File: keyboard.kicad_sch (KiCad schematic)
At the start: 77 parts

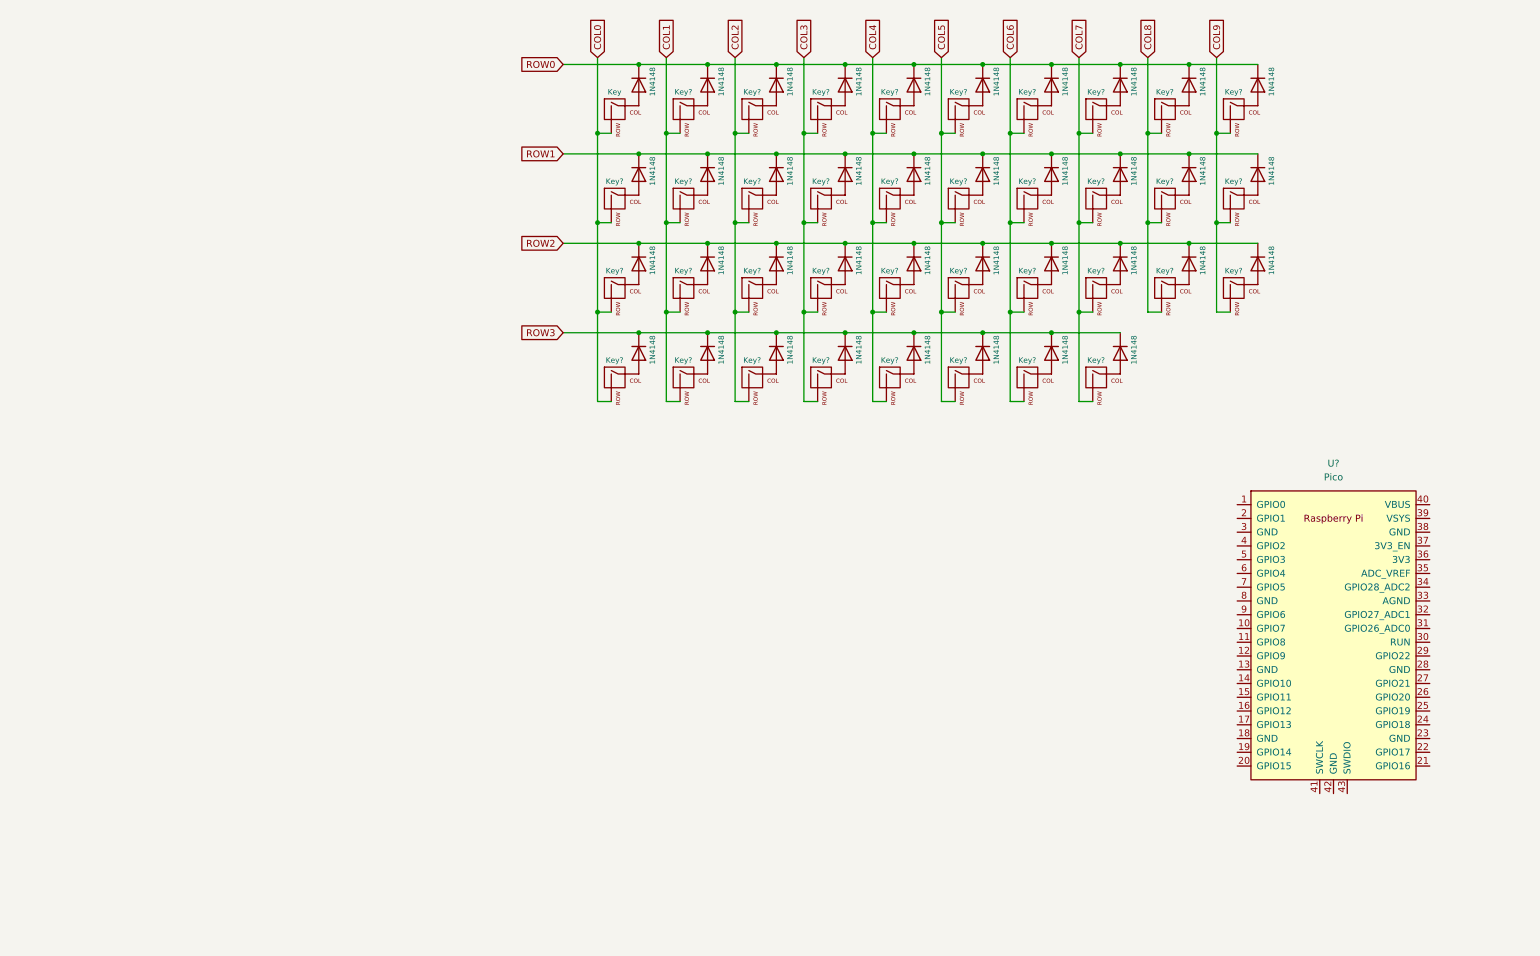
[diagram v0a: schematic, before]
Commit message: updated schematic to dual pallel switches
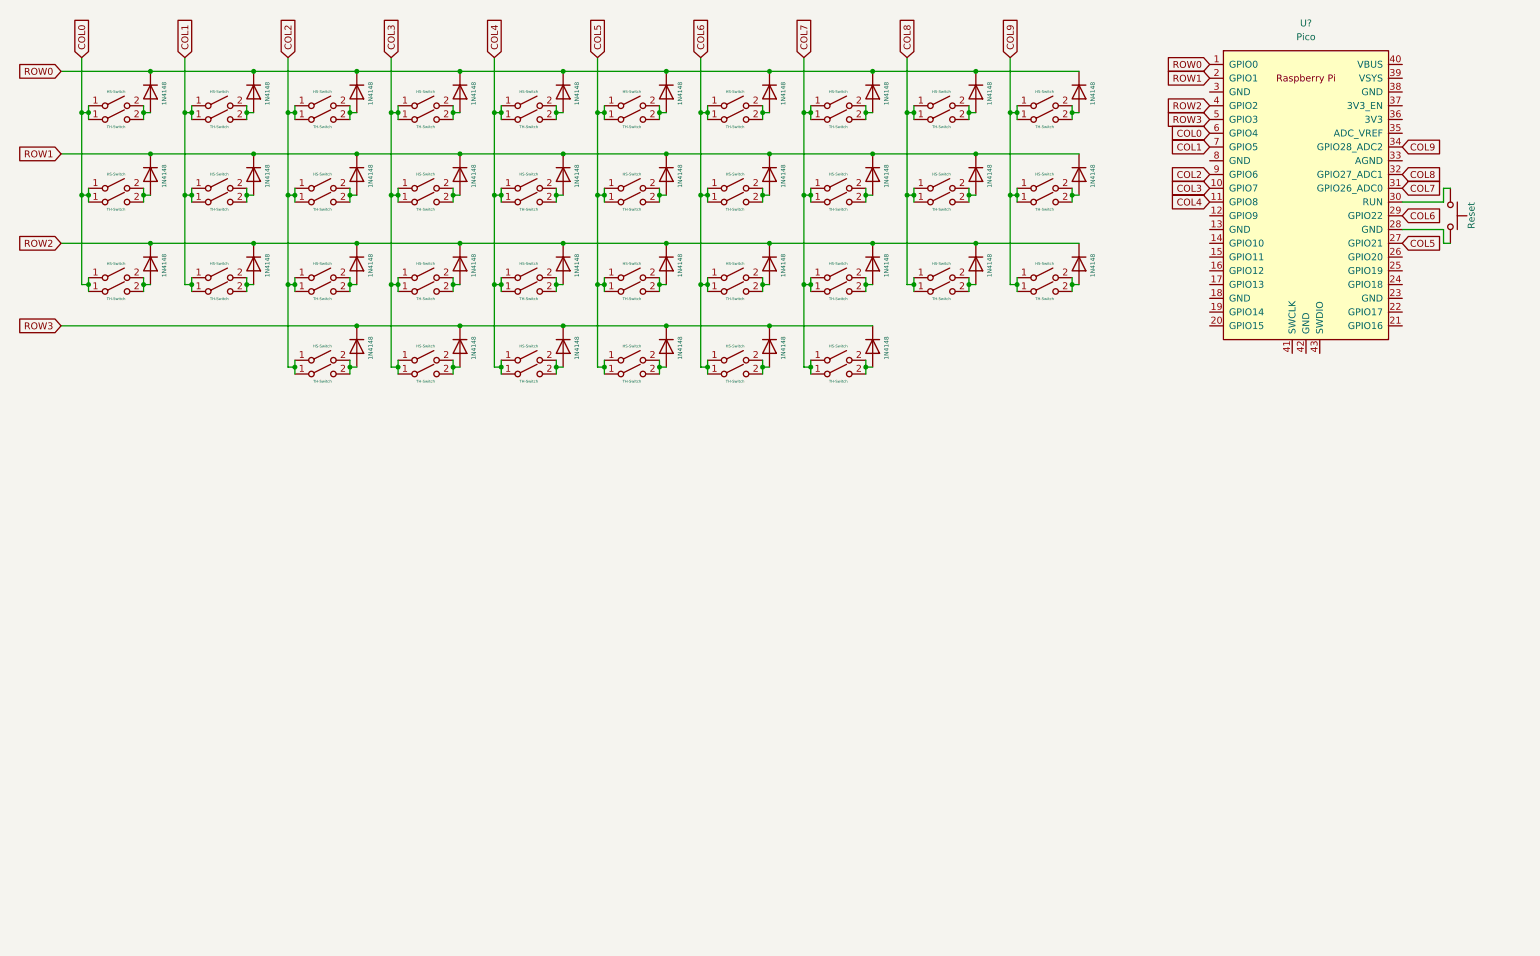
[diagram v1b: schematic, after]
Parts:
- removed D? (x38): 1N4148, Diode_THT:D_DO-35_SOD27_P7.62mm_Horizontal, symbol Diode:1N4148
- removed Key, Key? (x37): no-led, symbol MX_Alps_Hybrid:MX-NoLED
- added D? (x36): 1N4148, Diode_THT:D_DO-35_SOD27_P7.62mm_Horizontal, symbol Diode:1N4148
- added Reset: SW_Push, symbol Switch:SW_Push
- added SW? (x36): HS-Switch, symbol Switch:SW_SPST
- added SW? (x36): TH-Switch, symbol Switch:SW_SPST
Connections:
- net COL0: now also U?.6 (GPIO4), SW?.1 (A), SW?.1 (A), SW?.1 (A), SW?.1 (A), SW?.1 (A), SW?.1 (A)
- net COL1: now also U?.7 (GPIO5), SW?.1 (A), SW?.1 (A), SW?.1 (A), SW?.1 (A), SW?.1 (A), SW?.1 (A)
- net COL2: now also U?.9 (GPIO6), SW?.1 (A), SW?.1 (A), SW?.1 (A), SW?.1 (A), SW?.1 (A), SW?.1 (A), SW?.1 (A), SW?.1 (A)
- net COL3: now also U?.10 (GPIO7), SW?.1 (A), SW?.1 (A), SW?.1 (A), SW?.1 (A), SW?.1 (A), SW?.1 (A), SW?.1 (A), SW?.1 (A)
- net COL4: now also U?.11 (GPIO8), SW?.1 (A), SW?.1 (A), SW?.1 (A), SW?.1 (A), SW?.1 (A), SW?.1 (A), SW?.1 (A), SW?.1 (A)
- net COL5: now also U?.27 (GPIO21), SW?.1 (A), SW?.1 (A), SW?.1 (A), SW?.1 (A), SW?.1 (A), SW?.1 (A), SW?.1 (A), SW?.1 (A)
- net COL6: now also U?.29 (GPIO22), SW?.1 (A), SW?.1 (A), SW?.1 (A), SW?.1 (A), SW?.1 (A), SW?.1 (A), SW?.1 (A), SW?.1 (A)
- net COL7: now also U?.31 (GPIO26_ADC0), SW?.1 (A), SW?.1 (A), SW?.1 (A), SW?.1 (A), SW?.1 (A), SW?.1 (A), SW?.1 (A), SW?.1 (A)
- net COL8: now also U?.32 (GPIO27_ADC1), SW?.1 (A), SW?.1 (A), SW?.1 (A), SW?.1 (A), SW?.1 (A), SW?.1 (A)
- net COL9: now also U?.34 (GPIO28_ADC2), SW?.1 (A), SW?.1 (A), SW?.1 (A), SW?.1 (A), SW?.1 (A), SW?.1 (A)
- net ROW0: now also U?.1 (GPIO0), D?.1 (K), D?.1 (K), D?.1 (K), D?.1 (K), D?.1 (K), D?.1 (K), D?.1 (K), D?.1 (K), D?.1 (K), D?.1 (K)
- net ROW1: now also U?.2 (GPIO1), D?.1 (K), D?.1 (K), D?.1 (K), D?.1 (K), D?.1 (K), D?.1 (K), D?.1 (K), D?.1 (K), D?.1 (K), D?.1 (K)
- net ROW2: now also U?.4 (GPIO2), D?.1 (K), D?.1 (K), D?.1 (K), D?.1 (K), D?.1 (K), D?.1 (K), D?.1 (K), D?.1 (K), D?.1 (K), D?.1 (K)
- net ROW3: now also U?.5 (GPIO3), D?.1 (K), D?.1 (K), D?.1 (K), D?.1 (K), D?.1 (K), D?.1 (K)
- net at U?.28 (GND): now also Reset.2
- net at U?.30 (RUN): now also Reset.1
- new net: D?.2 (A), SW?.2 (B), SW?.2 (B) (x36)
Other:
- moved on the sheet: U?

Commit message: wired up 2 oled screens and 2 rotary encoders and cleaned up the schematic
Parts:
- added 10K (x6): R, symbol Device:R
- added Brd?: OLEDR, symbol SSD1306-128x64_OLED:SSD1306
- added Brd?: OLEDL, symbol SSD1306-128x64_OLED:SSD1306
- added SW?: RER, symbol Device:RotaryEncoder_Switch
- added SW?: REL, symbol Device:RotaryEncoder_Switch
- U?: value Pico -> Pi Pico
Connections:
- net REL-S1: now reaches U?.12 (GPIO9)
- net REL-S1: now also 10K.1, SW?.S1
- net REL-A: now reaches U?.14 (GPIO10)
- net REL-A: now also 10K.2, SW?.A
- net REL-B: now reaches U?.15 (GPIO11)
- net REL-B: now also 10K.2, SW?.B
- net SDAOLEDL: now reaches U?.16 (GPIO12)
- net SDAOLEDL: now also Brd?.4 (SDA)
- net SCLOLEDL: now reaches U?.17 (GPIO13)
- net SCLOLEDL: now also Brd?.3 (SCL)
- net SDAOLEDR: now reaches U?.21 (GPIO16)
- net SDAOLEDR: now also Brd?.4 (SDA)
- net SCLOLEDR: now reaches U?.22 (GPIO17)
- net SCLOLEDR: now also Brd?.3 (SCL)
- net REGND: now reaches U?.23 (GND)
- net REGND: now also SW?.C, SW?.C, SW?.S2, SW?.S2
- net RER-B: now reaches U?.24 (GPIO18)
- net RER-B: now also 10K.2, SW?.B
- net RER-A: now reaches U?.25 (GPIO19)
- net RER-A: now also 10K.2, SW?.A
- net RER-S1: now reaches U?.26 (GPIO20)
- net RER-S1: now also 10K.1, SW?.S1
- net RE3V3: now reaches U?.36 (3V3)
- net RE3V3: now also 10K.1, 10K.1, 10K.1, 10K.1, 10K.2, 10K.2
- net OLEDGND: now reaches U?.38 (GND)
- net OLEDGND: now also Brd?.1 (GND), Brd?.1 (GND)
- net OLED: now reaches U?.40 (VBUS)
- net OLED: now also Brd?.2 (VCC), Brd?.2 (VCC)
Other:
- moved on the sheet: Reset
